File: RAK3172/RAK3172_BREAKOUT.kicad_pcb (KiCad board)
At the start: 2 copper layers, 29.4 x 36.8 mm, 5 parts, among them J1 Conn_01x14_Male, J2 Conn_01x14_Male, J3 Conn_01x14_Male, U1 RAK3712

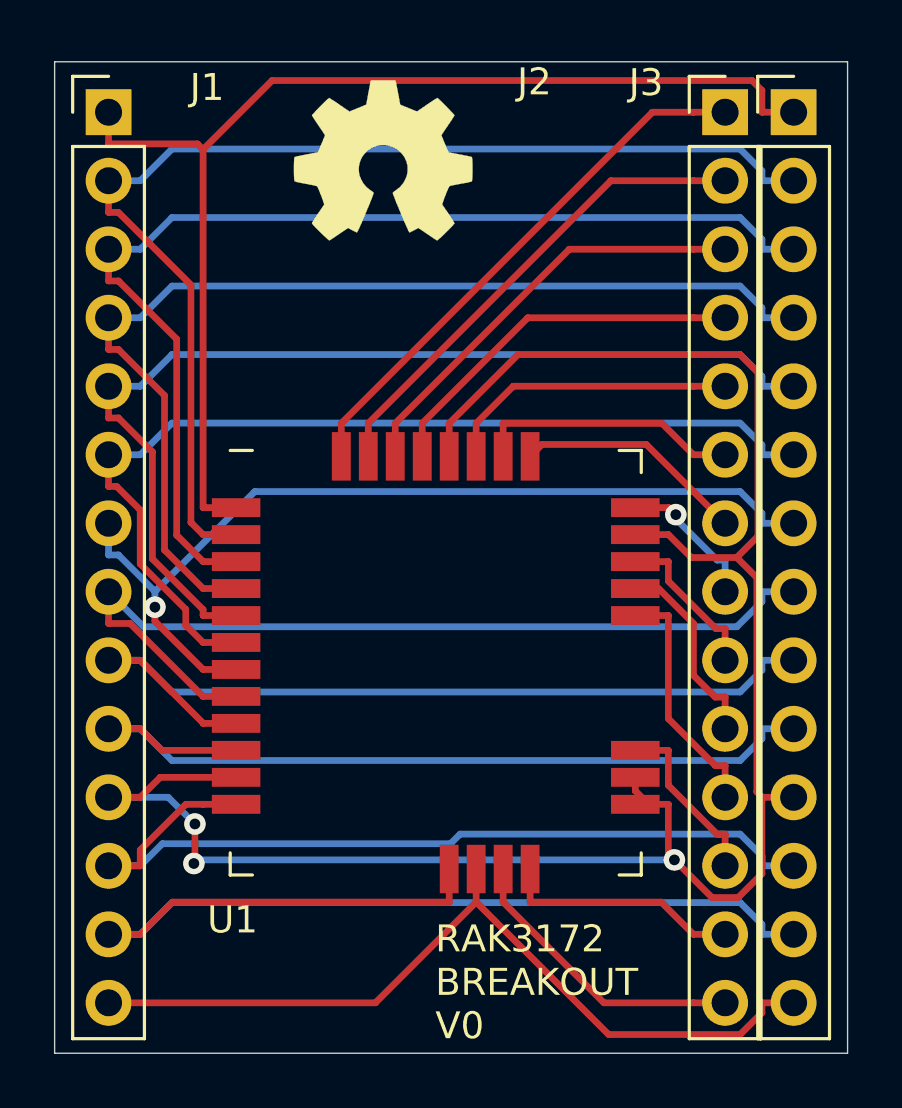
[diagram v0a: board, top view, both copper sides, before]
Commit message: proj:(DIL_BREAKOUT_PCB RAK 3712)changed project filenames
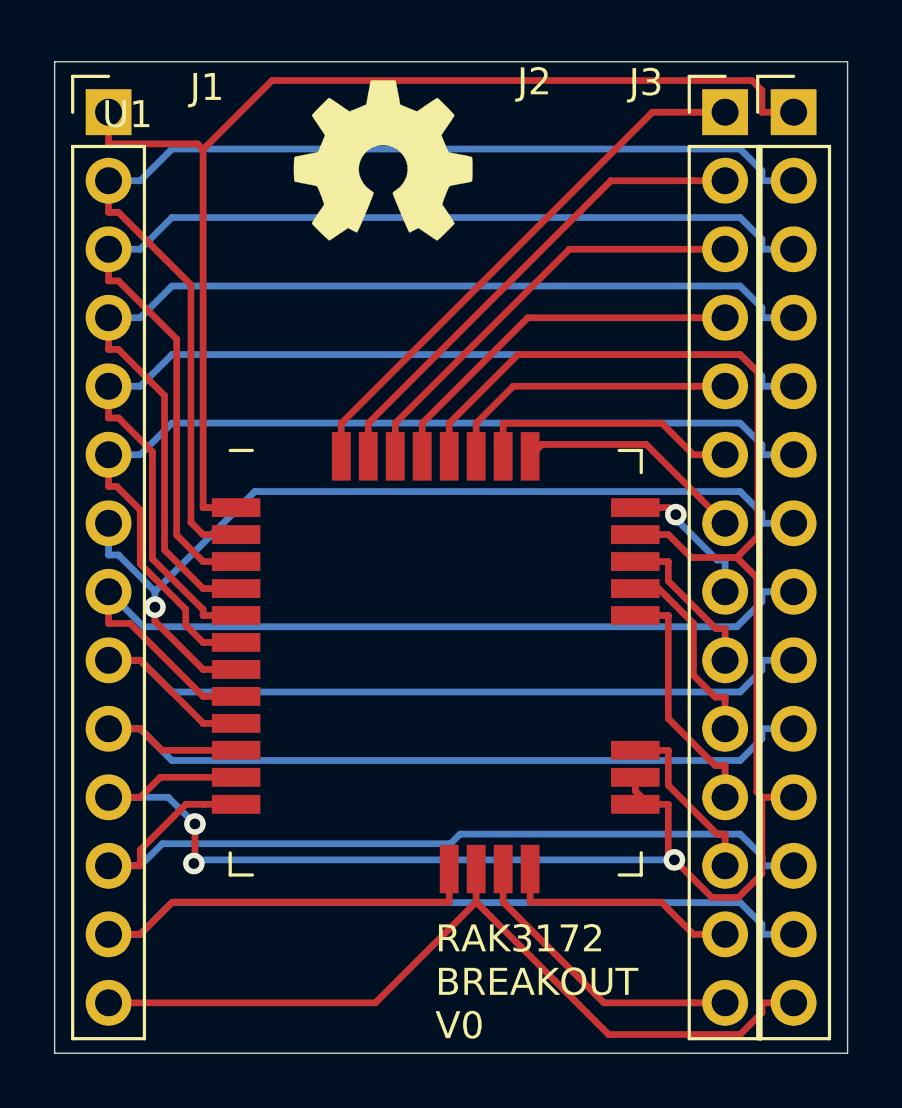
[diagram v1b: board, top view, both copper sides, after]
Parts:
- U1: value RAK3712 -> RAK3172; footprint RAKWIRELESS:RAK3712 -> RAKWIRELESS:RAK3172
